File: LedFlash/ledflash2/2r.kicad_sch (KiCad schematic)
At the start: 3 parts

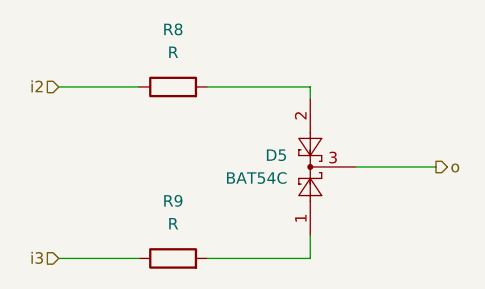
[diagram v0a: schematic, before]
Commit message: Update LED Flash - Added R values, tables and BOM file
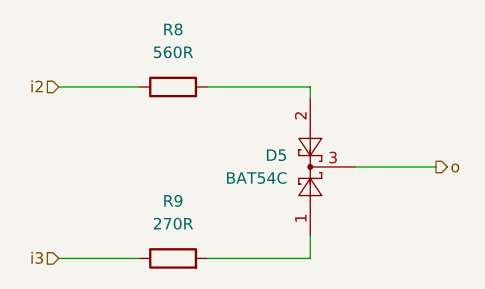
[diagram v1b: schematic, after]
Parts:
- R8: value R -> 560R
- R9: value R -> 270R
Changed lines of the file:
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@@
 			)
 		)
-		(property "Value" "R"
+		(property "Value" "270R"
 			(at 149.86 119.38 90)
 			(effects
@@
 			)
 		)
-		(property "Value" "R"
+		(property "Value" "560R"
 			(at 149.86 100.33 90)
 			(effects
